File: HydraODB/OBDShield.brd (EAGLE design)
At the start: 59.9 x 37 mm, 23 parts, among them CN1 8p-2.54, J1 HYDRABUS_SHIELD_CON_HEADER_2X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, J2 HYDRABUS_SHIELD_CON_HEADER_2X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, J3 HYDRABUS_SHIELD_CON_HEADER_2X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, K1 TS-1188E, U1 SN65HVD233DG4, U2 SN65HVD233DG4, U3 CJ78M05-to252

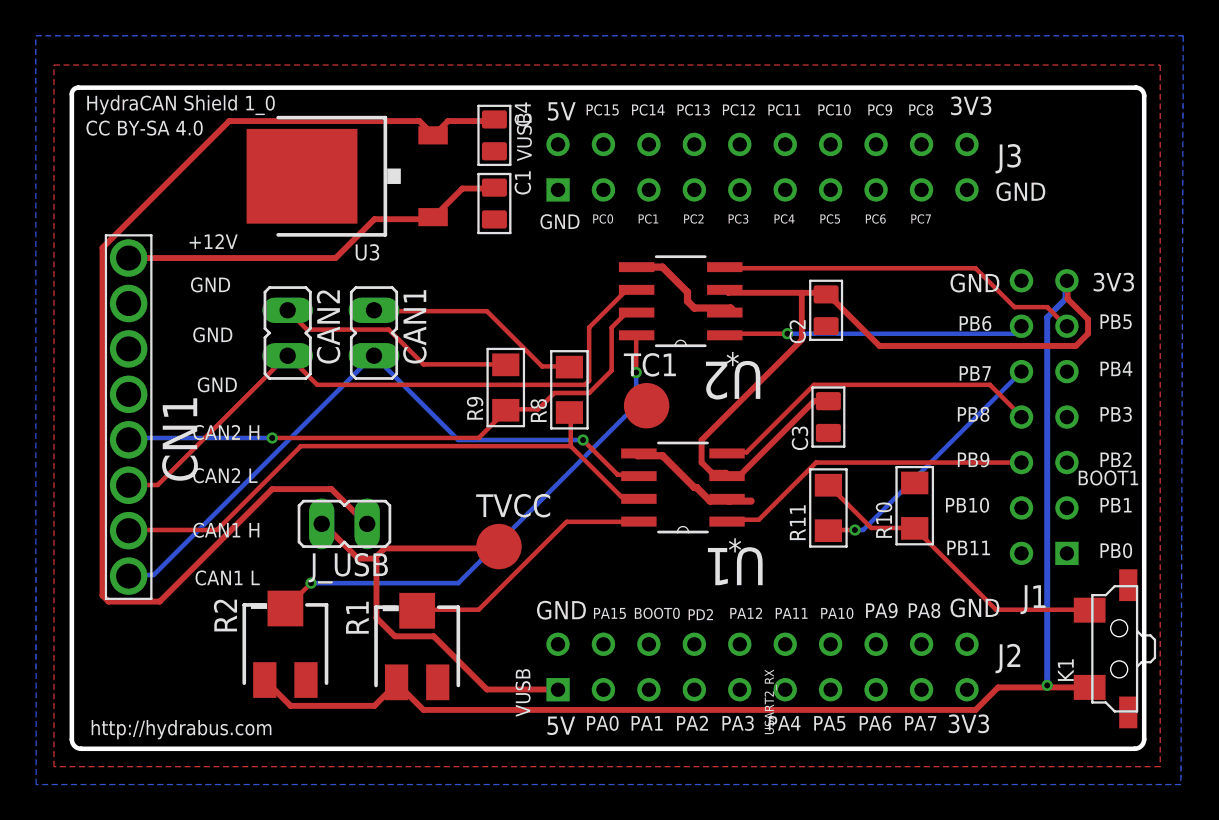
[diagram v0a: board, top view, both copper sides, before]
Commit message: Added 2 LIN Bus transceivers
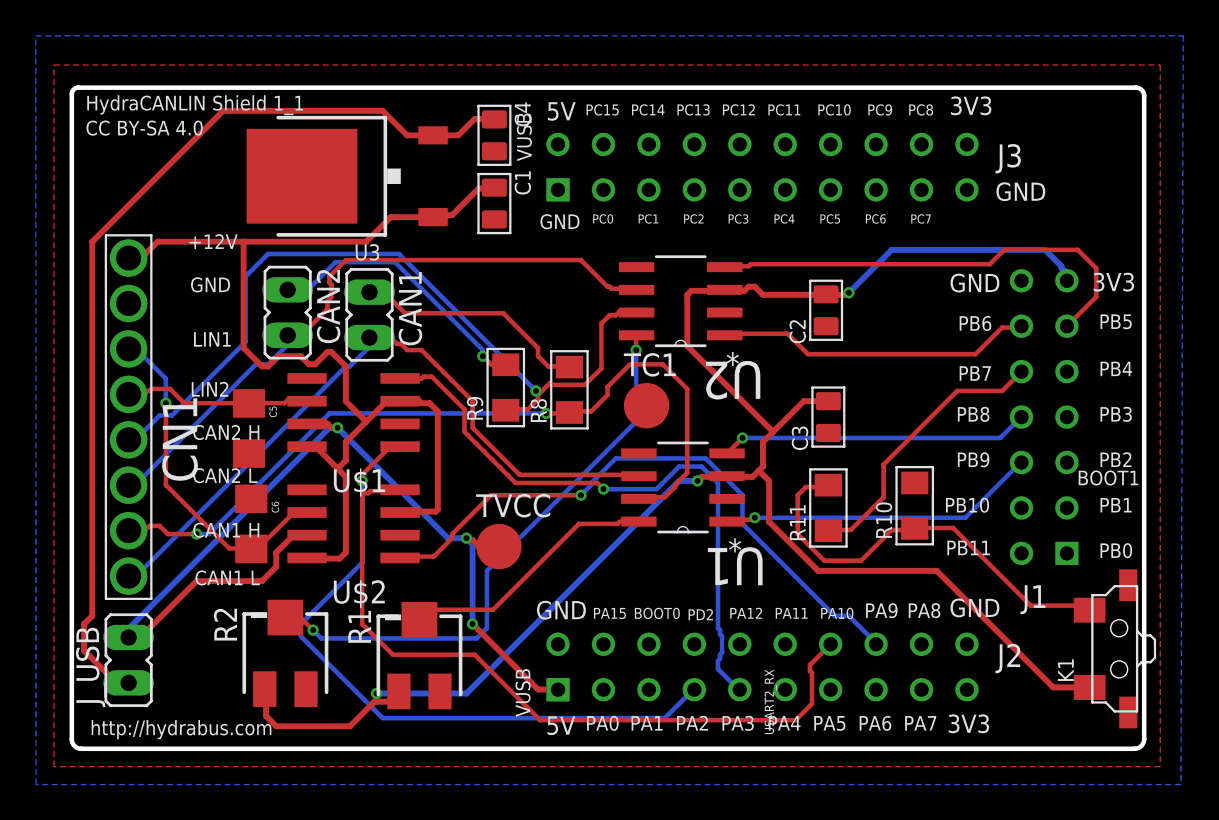
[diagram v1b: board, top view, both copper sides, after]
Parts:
- added C5, C6: (no value), _c2h:1206
- added U$1, U$2: TJA1020SO8, nxp:SO8
- moved J_USB 14.3 mm to (3.17, 4.95), turned to 0 degrees
- moved CAN2 1.14 mm to (12.1, 24.4)
- moved CAN1 1.05 mm to (16.6, 24.3)
- moved R1 0.52 mm to (19.4, 5.21)
- moved R2 0.51 mm to (11.9, 5.33)
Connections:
- new net N$4: C5.1, CN1.5, U$1.6
- new net N$7: C6.2, CN1.6, U$2.6
- net +12V: now also U$1.3, U$1.8, U$2.3, U$2.8
- net GND: now also C5.2, C6.1, U$1.5, U$2.5; no longer CN1.5, CN1.6
- net PA10: now also U$2.4
- net PA2: now also U$1.1
- net PA3: now also U$1.4
- net PA9: now also U$2.1
- net VCC/2: now also U$1.7, U$2.7
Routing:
- net +12V: track 22.1 -> 64.0 mm
- net PA10: track 0.00 -> 41.1 mm
- net PA2: track 0.00 -> 37.8 mm, vias 0 -> 1
- net PA9: track 0.00 -> 34.4 mm, vias 0 -> 1
- net PA3: track 0.00 -> 34.3 mm, vias 0 -> 1
- net VCC/2: track 26.2 -> 54.5 mm, vias 0 -> 3
- net N$7: track 0.00 -> 19.0 mm, vias 0 -> 1
- net +3V3: track 118.0 -> 101.6 mm, vias 1 -> 3
- net GND: track 14.6 -> 0.00 mm
- net N$12: track 32.8 -> 44.1 mm
- net N$10: track 33.6 -> 44.4 mm, vias 0 -> 2
- net N$4: track 0.00 -> 10.6 mm
- net N$15: track 63.3 -> 52.7 mm
- net N$21: track 17.5 -> 23.8 mm
- net PB5: track 20.5 -> 25.5 mm
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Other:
- board text added: "HydraCANLIN Shield 1_1"
- board text added: "LIN1"
- board text added: "LIN2"
- board text removed: "HydraCAN Shield 1_0"

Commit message: Pullups for LIN transceivers
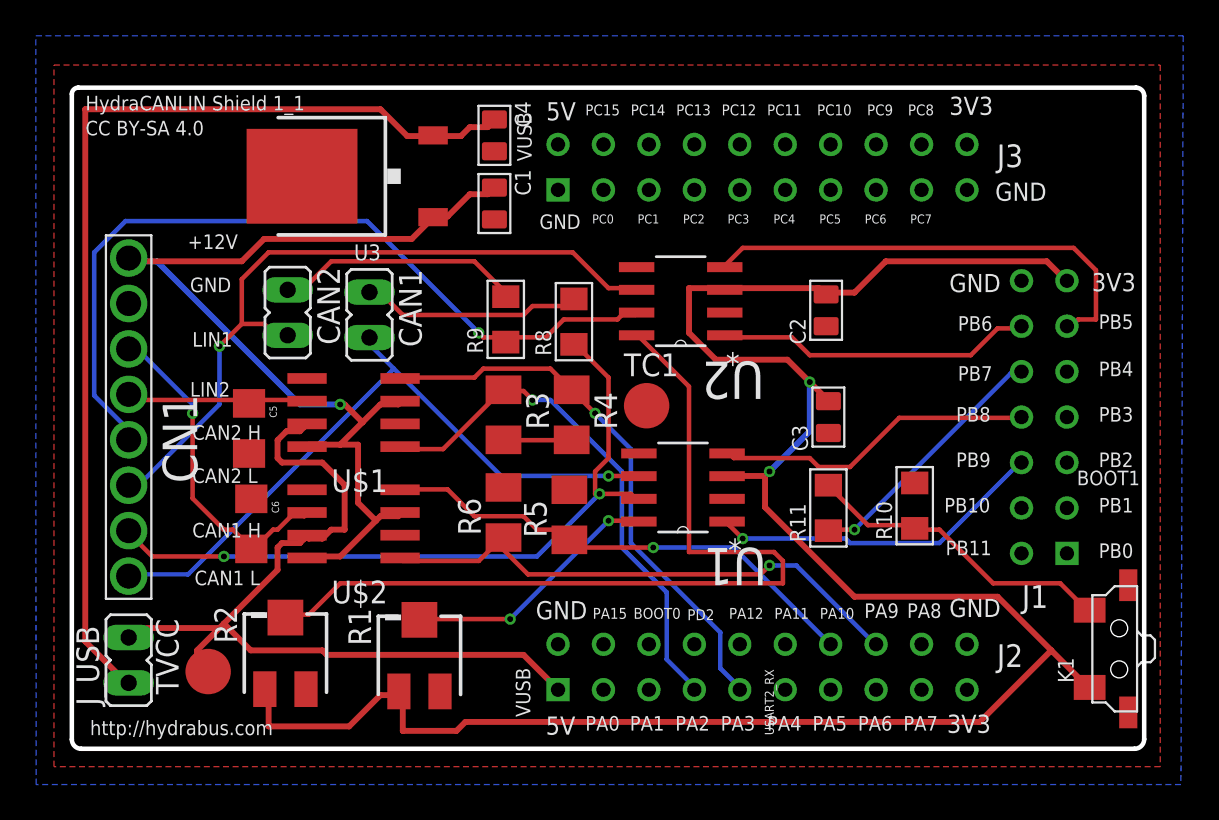
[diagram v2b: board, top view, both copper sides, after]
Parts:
- added R3, R4, R5, R6: (no value), resistor:M1206
- moved TVCC 17.7 mm to (7.62, 4.32), turned to 90 degrees
- moved R8 3.82 mm to (28.1, 23.9)
- moved R9 3.81 mm to (24.3, 24.0)
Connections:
- new net N$13: R3.2, R4.2
- new net N$18: R6.2
- net PA10: now also R5.1
- net PA2: now also R3.1
- net PA3: now also R4.1
- net PA9: now also R6.1
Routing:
- net N$17: track 31.8 -> 48.7 mm, vias 2 -> 0
- net +3V3: track 101.6 -> 117.8 mm, vias 3 -> 2
- net PA10: track 41.1 -> 27.7 mm, vias 0 -> 1
- net PA2: track 37.8 -> 29.6 mm
- net +12V: track 64.0 -> 57.4 mm, vias 0 -> 1
- net N$21: track 23.8 -> 17.5 mm
- net VCC/2: track 54.5 -> 49.1 mm, vias 3 -> 0
- net N$11: track 35.8 -> 40.9 mm, vias 0 -> 1
- net N$15: track 52.7 -> 57.0 mm
- net N$10: track 44.4 -> 40.5 mm
- net N$13: track 0.00 -> 3.81 mm
- net PA9: track 34.4 -> 30.8 mm
- net PA3: track 34.3 -> 30.9 mm
- net N$12: track 44.1 -> 46.8 mm
- net N$16: track 15.4 -> 13.8 mm, vias 1 -> 0
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
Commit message: corrections on ground plate
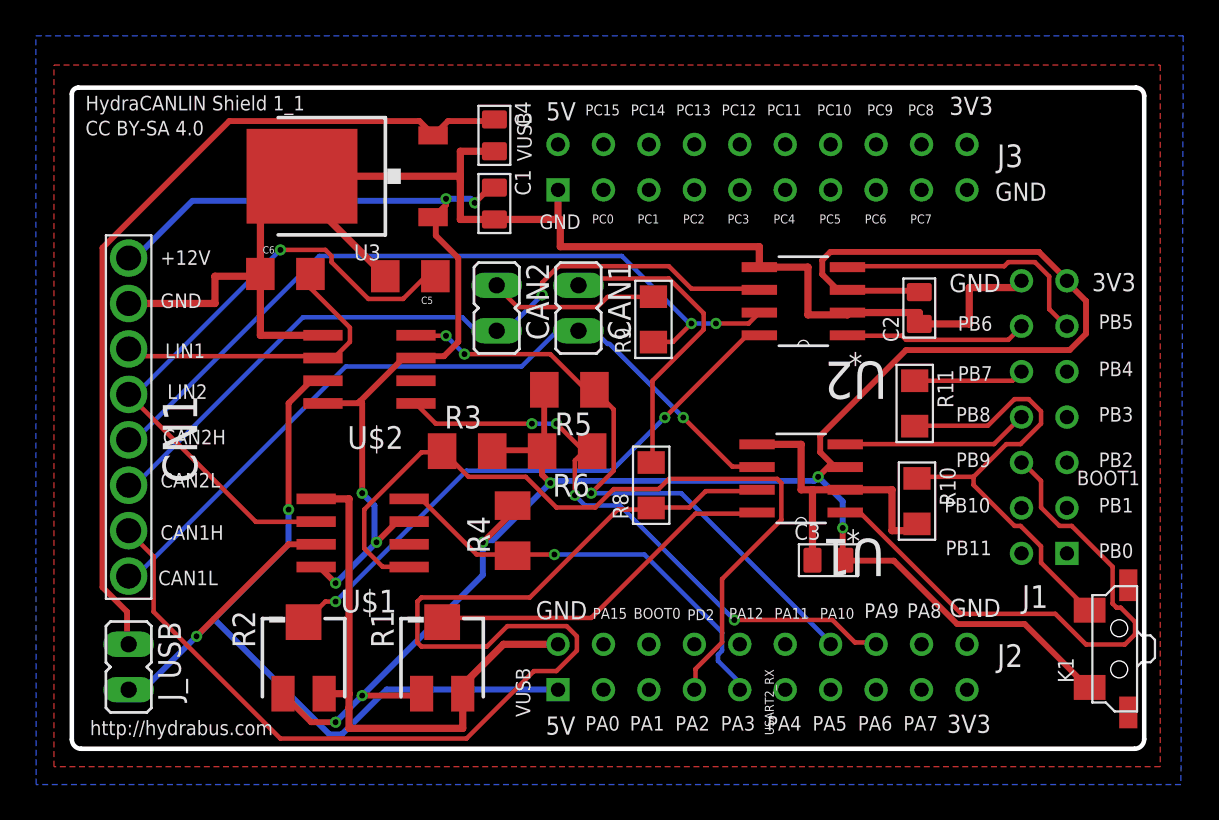
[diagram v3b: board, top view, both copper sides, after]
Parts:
- removed TC1, TVCC: TPB2,54, testpad:B2,54
- moved C6 14.1 mm to (11.9, 26.5), turned to 0 degrees
- moved C5 12.4 mm to (18.9, 26.4), turned to 180 degrees
- moved CAN1 11.7 mm to (28.3, 24.6)
- moved CAN2 11.7 mm to (23.7, 24.6)
- moved R8 10.1 mm to (32.4, 14.7)
- moved U$2 8.68 mm to (16.6, 21.2)
- moved R9 8.25 mm to (32.5, 24.0)
- moved C3 8.00 mm to (42.3, 10.5), turned to 90 degrees
- moved R11 7.58 mm to (47.1, 19.3), turned to 270 degrees
- moved R4 7.27 mm to (24.6, 12.2), turned to 90 degrees
- moved R5 6.98 mm to (27.8, 20.1), turned to 180 degrees
- moved U2 6.86 mm to (40.9, 25.0)
- moved U$1 6.75 mm to (16.3, 12.1)
- moved U1 6.62 mm to (40.8, 15.1)
- moved C2 5.21 mm to (47.4, 24.6)
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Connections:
- removed net N$13: R3.2, R4.2
- removed net N$18: R6.2
- net +3V3: now also R3.2, R4.2, R5.2, R6.2
- net GND: no longer TC1.TP
- net VCC/2: no longer TVCC.TP
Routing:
- net GND: track 0.00 -> 138.2 mm
- net N$10: track 40.5 -> 68.2 mm, vias 2 -> 0
- net N$4: track 10.3 -> 35.8 mm, vias 0 -> 1
- net N$17: track 48.7 -> 32.1 mm, vias 0 -> 2
- net PA2: track 29.6 -> 45.5 mm, vias 1 -> 0
- net PB10: track 18.8 -> 32.3 mm, vias 1 -> 0
- net PB5: track 26.3 -> 14.9 mm
- net N$21: track 17.5 -> 27.2 mm
- net N$15: track 57.0 -> 48.3 mm
- net PB7: track 14.5 -> 6.18 mm, vias 1 -> 0
- net PB11: track 17.8 -> 10.2 mm
- net PB8: track 17.9 -> 10.5 mm
- net PA10: track 27.7 -> 34.9 mm, vias 1 -> 3
- net PA3: track 30.9 -> 24.5 mm
- net N$9: track 38.2 -> 44.0 mm
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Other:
- board text added: "CAN1H"
- board text added: "CAN1L"
- board text added: "CAN2H"
- board text added: "CAN2L"
- board text removed: "CAN1 H"
- board text removed: "CAN1 L"
- board text removed: "CAN2 H"
- board text removed: "CAN2 L"
